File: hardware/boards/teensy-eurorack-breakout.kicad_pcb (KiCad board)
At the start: 2 copper layers, 110.5 x 111.1 mm, 74 parts, among them J1 Conn_01x08, SW1 Rotary_Encoder_Switch, SW2 Rotary_Encoder_Switch, SW3 Rotary_Encoder_Switch, U2 AD5754BREZ, U3 AD5754BREZ, U5 MCP1700-2502E, U6 AD7606BSTZ, U7 6N138

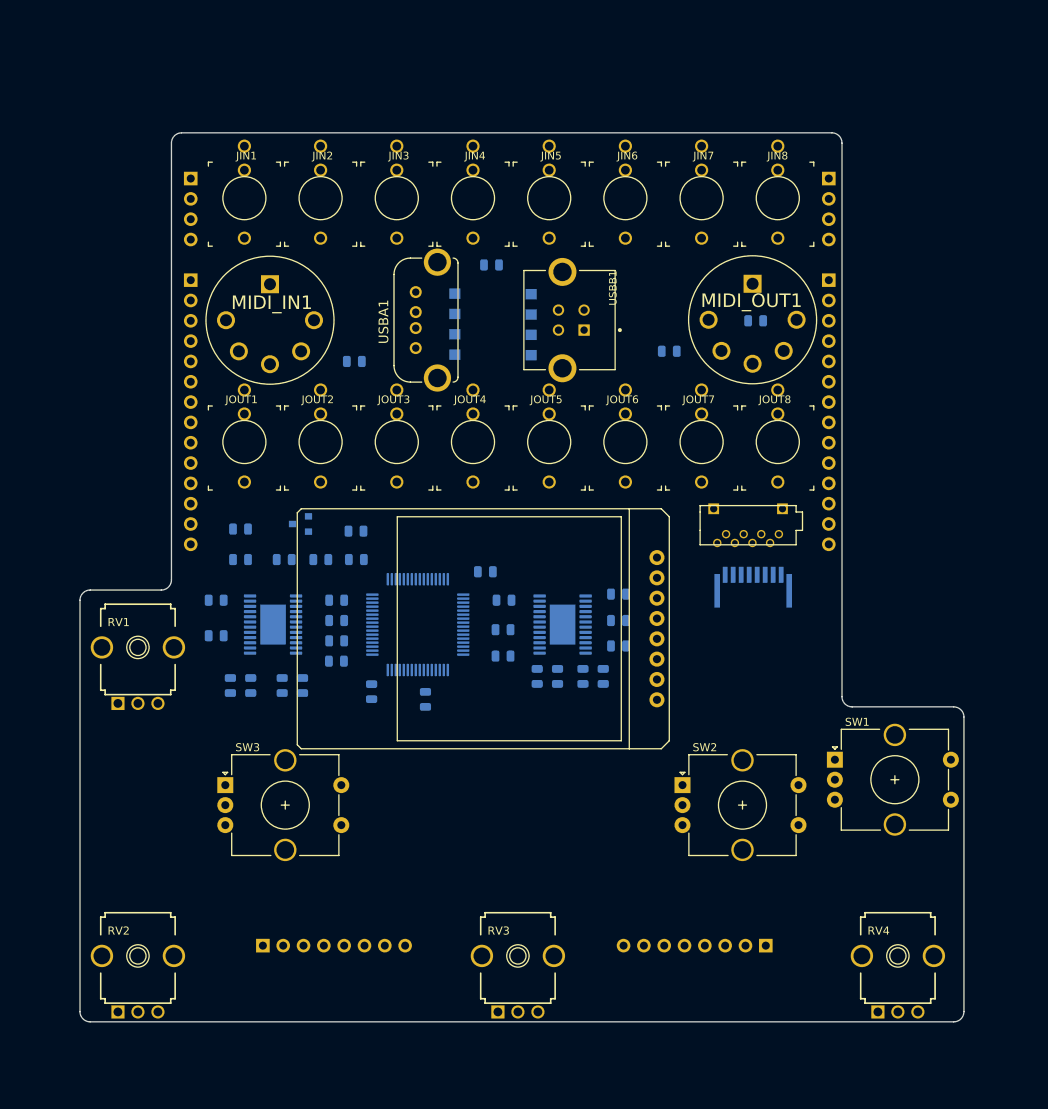
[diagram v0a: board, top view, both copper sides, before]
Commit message: breakout DRC'ed
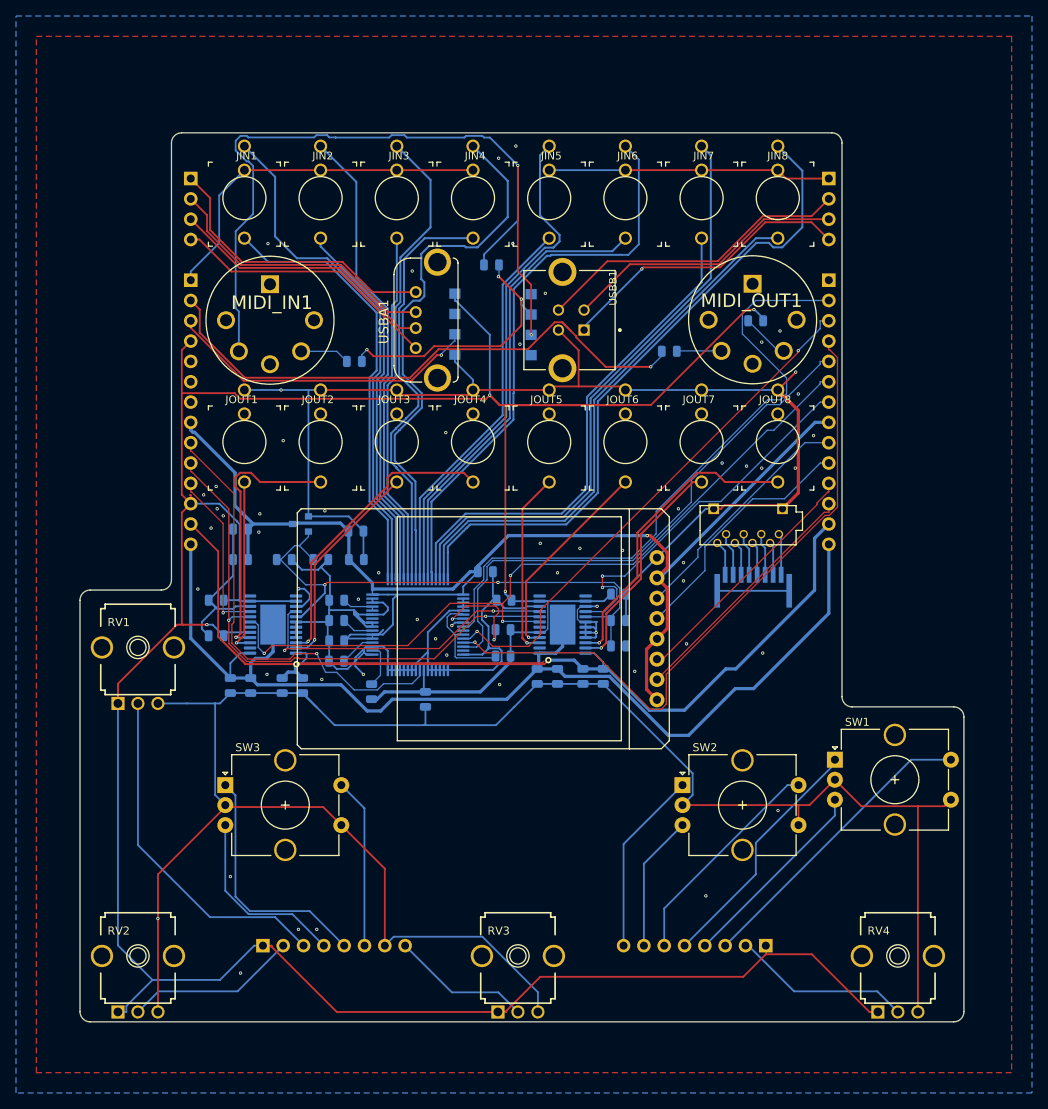
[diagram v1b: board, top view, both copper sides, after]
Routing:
- net GND: track 0.00 -> 657.0 mm, vias 0 -> 58
- net +3V3: track 0.00 -> 418.4 mm, vias 0 -> 4
- net +5V: track 0.00 -> 168.6 mm, vias 0 -> 1
- net +12V: track 0.00 -> 167.4 mm, vias 0 -> 2
- net -12V: track 0.00 -> 137.3 mm
- net Net-(D1-Pad2): track 0.00 -> 102.1 mm, vias 0 -> 2
- net /DAC_SYNC: track 0.00 -> 98.2 mm, vias 0 -> 3
- net /ADC_CS: track 0.00 -> 84.2 mm, vias 0 -> 1
- net /VGND8: track 0.00 -> 84.1 mm
- net /ADC_CONVST: track 0.00 -> 81.7 mm
- net /VGND7: track 0.00 -> 75.7 mm
- net /MIDI_TX: track 0.00 -> 72.5 mm, vias 0 -> 1
- net /VGND6: track 0.00 -> 71.5 mm
- net /DAC_REF2V5: track 0.00 -> 70.7 mm, vias 0 -> 2
- net /DAC_SCK: track 0.00 -> 69.7 mm, vias 0 -> 2
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- added copper zone on B.Cu, net GND
- added copper zone on F.Cu, net GND
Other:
- net class Default: clearance 0.2 -> 0.1524; trace_width 0.25 -> 0.1524
- rule trace_clearance: 0.2 -> 0.1524
- rule trace_min: 0.2 -> 0.1524
- rule via_min_drill: 0.3 -> 0.1016
- rule via_min_size: 0.4 -> 0.2032

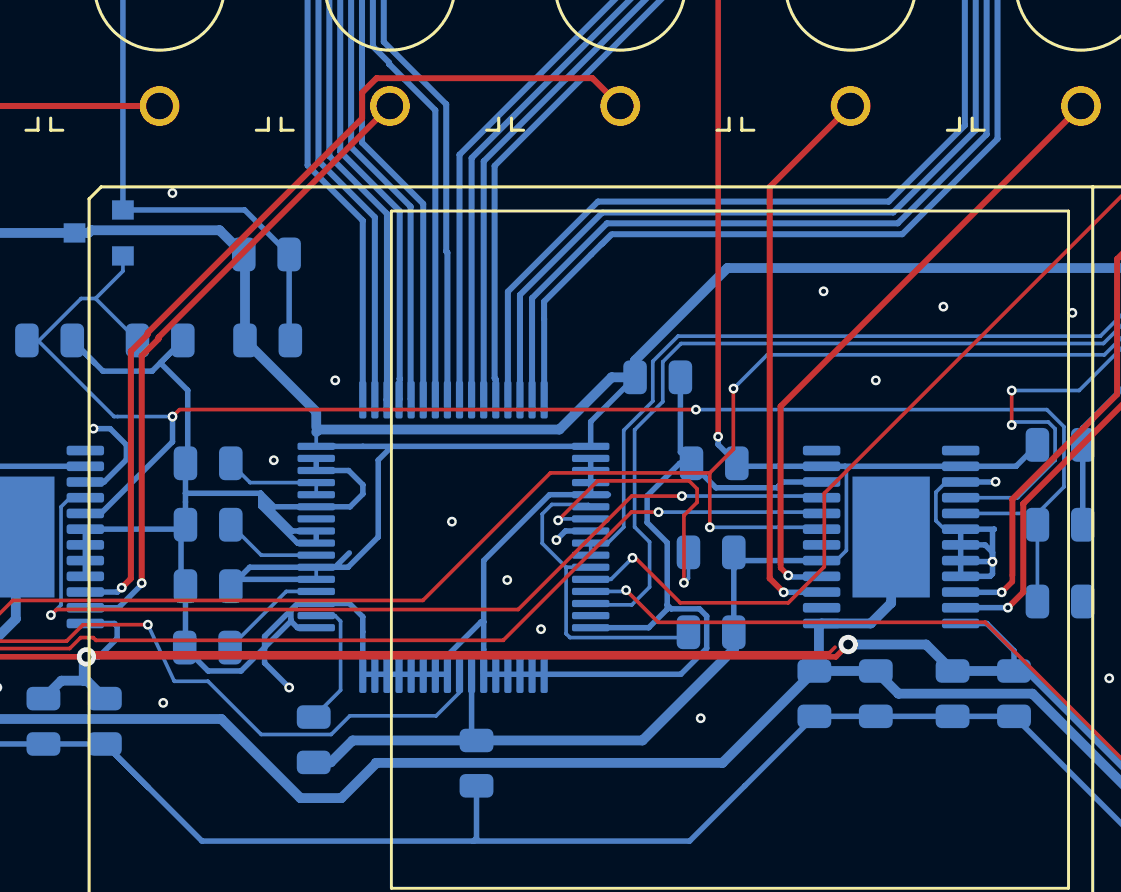
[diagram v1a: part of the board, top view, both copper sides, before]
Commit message: minor tweeks to breakout board
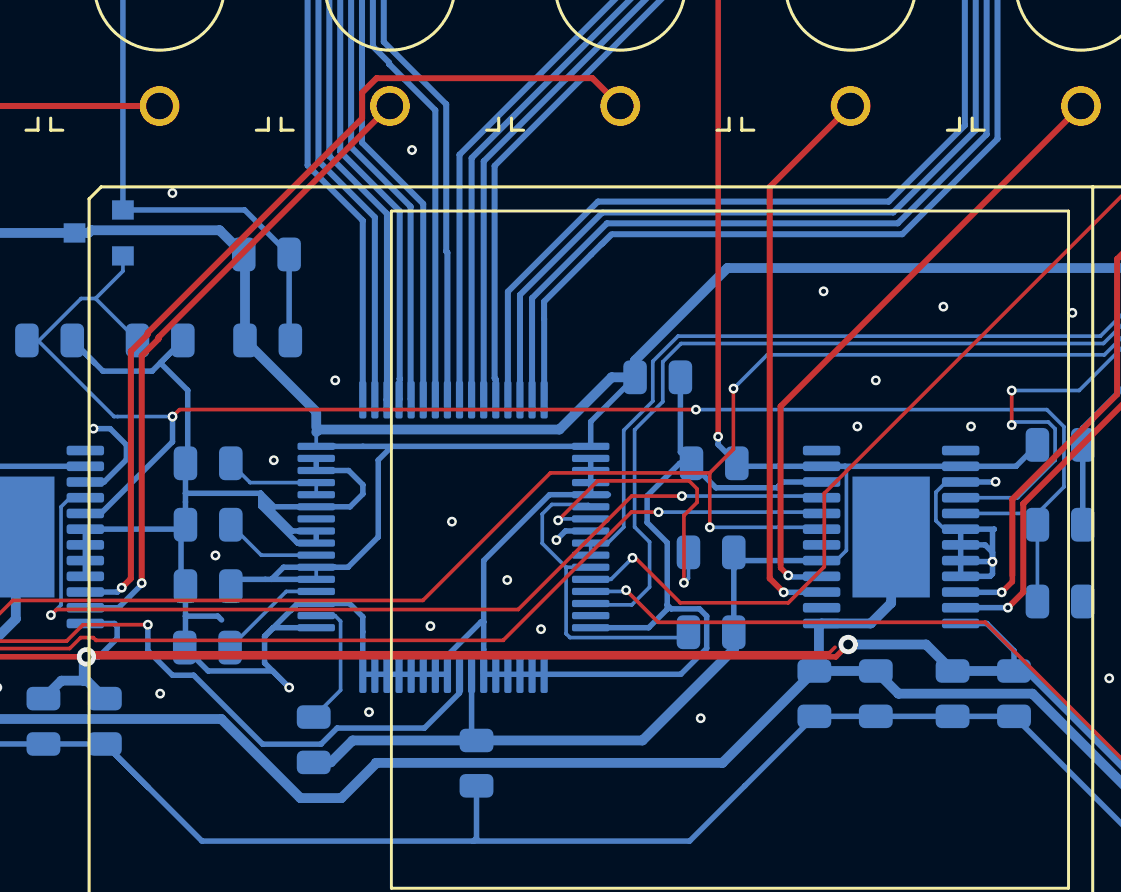
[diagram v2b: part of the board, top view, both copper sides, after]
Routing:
- net +5V: track 168.6 -> 165.1 mm
- net GND: track 657.0 -> 658.6 mm, vias 58 -> 64
- net /ADC_MISO: track 55.9 -> 57.1 mm

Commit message: cleanup traces
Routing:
- net +12V: track 167.4 -> 142.2 mm
- net /ADC_CONVST: track 81.7 -> 73.1 mm
- net /DAC_SDIN: track 21.3 -> 25.5 mm
- net GND: track 658.6 -> 661.7 mm, vias 64 -> 66
- net /DAC_SDOUT: track 46.5 -> 49.5 mm
- net /DAC_SYNC: track 98.2 -> 101.0 mm
- net /DAC_SCK: track 69.7 -> 71.4 mm
- net /TFT_SCK: track 30.1 -> 31.7 mm
- net /ADC_BUSY: track 68.0 -> 69.1 mm
- net /TFT_DC: track 31.3 -> 32.1 mm
- net +3V3: track 418.4 -> 417.7 mm
- net -12V: track 137.3 -> 137.9 mm
- net /ADC_SCK: track 66.2 -> 65.6 mm

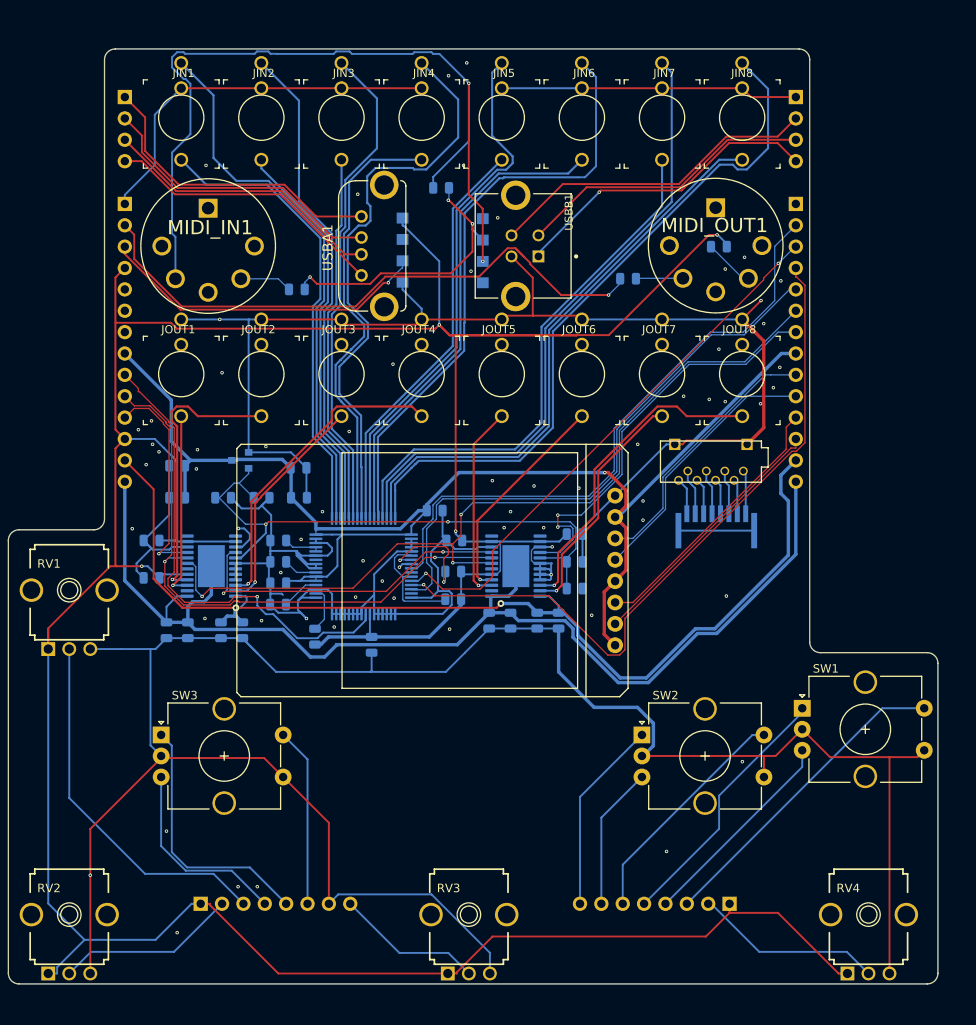
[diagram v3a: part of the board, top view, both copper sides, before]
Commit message: silkscreen improvments, gerbers, drc'ed
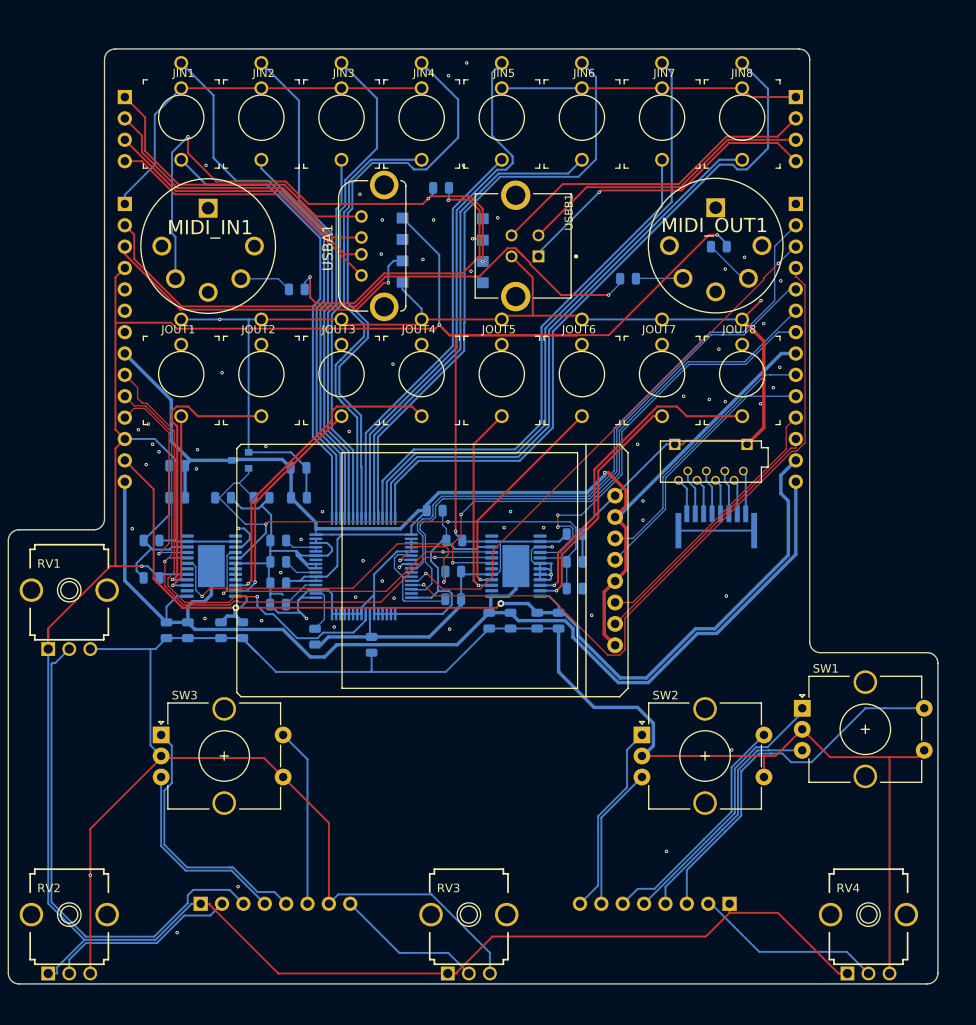
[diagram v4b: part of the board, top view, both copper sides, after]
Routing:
- net Net-(D1-Pad2): track 102.1 -> 66.0 mm, vias 2 -> 3
- net /P1: track 43.6 -> 59.2 mm
- net /ES1: track 37.8 -> 44.1 mm
- net /E1B: track 25.0 -> 28.1 mm
- net Net-(D1-Pad1): track 38.3 -> 40.5 mm
- net /ADC_BUSY: track 69.1 -> 70.3 mm
- net /ADC_CONVST: track 73.1 -> 74.2 mm
- net /P2: track 21.6 -> 22.6 mm
- net /E1A: track 31.0 -> 31.8 mm
- net /E3A: track 30.6 -> 31.3 mm
- net /MIDI_RX: track 39.6 -> 40.2 mm
- net GND: vias 66 -> 65

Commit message: recenter pcb in page
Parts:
- moved C19 235.5 mm to (140.5, 112.3)
- moved C20 235.5 mm to (144.9, 102.0)
- moved C21 235.5 mm to (102.9, 113.4)
- moved C22 235.5 mm to (94.6, 102.7)
- moved C23 235.5 mm to (143.0, 112.3)
- moved C24 235.5 mm to (130.6, 102.7)
- moved C25 235.5 mm to (105.4, 113.4)
- moved C26 235.5 mm to (94.6, 107.2)
- moved C27 235.5 mm to (97.7, 93.9)
- moved C28 235.5 mm to (97.7, 97.7)
- moved C29 235.5 mm to (107.7, 97.7)
- moved C30 235.5 mm to (103.1, 97.7)
- moved C31 235.5 mm to (96.4, 113.4)
- moved C32 235.5 mm to (134.7, 112.3)
- moved C33 235.5 mm to (137.3, 112.3)
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
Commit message: Revert "recenter pcb in page"
This reverts commit 40a09dfd2033d5d90cab69f8a1165afd283f11e8.
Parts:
- moved C19 235.5 mm to (222.2, -108.6)
- moved C20 235.5 mm to (226.7, -118.9)
- moved C21 235.5 mm to (184.7, -107.4)
- moved C22 235.5 mm to (176.4, -118.1)
- moved C23 235.5 mm to (224.8, -108.6)
- moved C24 235.5 mm to (212.4, -118.1)
- moved C25 235.5 mm to (187.2, -107.4)
- moved C26 235.5 mm to (176.4, -113.7)
- moved C27 235.5 mm to (179.5, -127.0)
- moved C28 235.5 mm to (179.5, -123.2)
- moved C29 235.5 mm to (189.5, -123.2)
- moved C30 235.5 mm to (184.9, -123.2)
- moved C31 235.5 mm to (178.2, -107.4)
- moved C32 235.5 mm to (216.5, -108.6)
- moved C33 235.5 mm to (219.1, -108.6)
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
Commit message: corrected edge on breakout board
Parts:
- moved JB2 230.4 mm to (176.8, 59.3)
- moved JB4 230.4 mm to (168.9, 142.5)
- moved JBUSBB1 230.4 mm to (176.8, 46.6)
- moved JIN7 230.4 mm to (160.9, 49.1)
- moved JIN8 230.4 mm to (170.4, 49.1)
- moved MIDI_OUT1 230.4 mm to (167.3, 64.3)
- moved R37 230.4 mm to (117.5, 69.5)
- moved RV4 230.4 mm to (185.4, 143.8)
- moved SW1 230.4 mm to (177.5, 119.3)
- moved C20 230.4 mm to (150.5, 98.6)
- moved C26 230.4 mm to (100.2, 103.8)
- moved C27 230.4 mm to (103.3, 90.4)
- moved C31 230.4 mm to (102.0, 110.0)
- moved C35 230.4 mm to (126.4, 111.7)
- moved C36 230.4 mm to (115.3, 104.4)
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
